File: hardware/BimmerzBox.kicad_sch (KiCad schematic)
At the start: 1 part, among them U2 ESP32-P4_MODULE

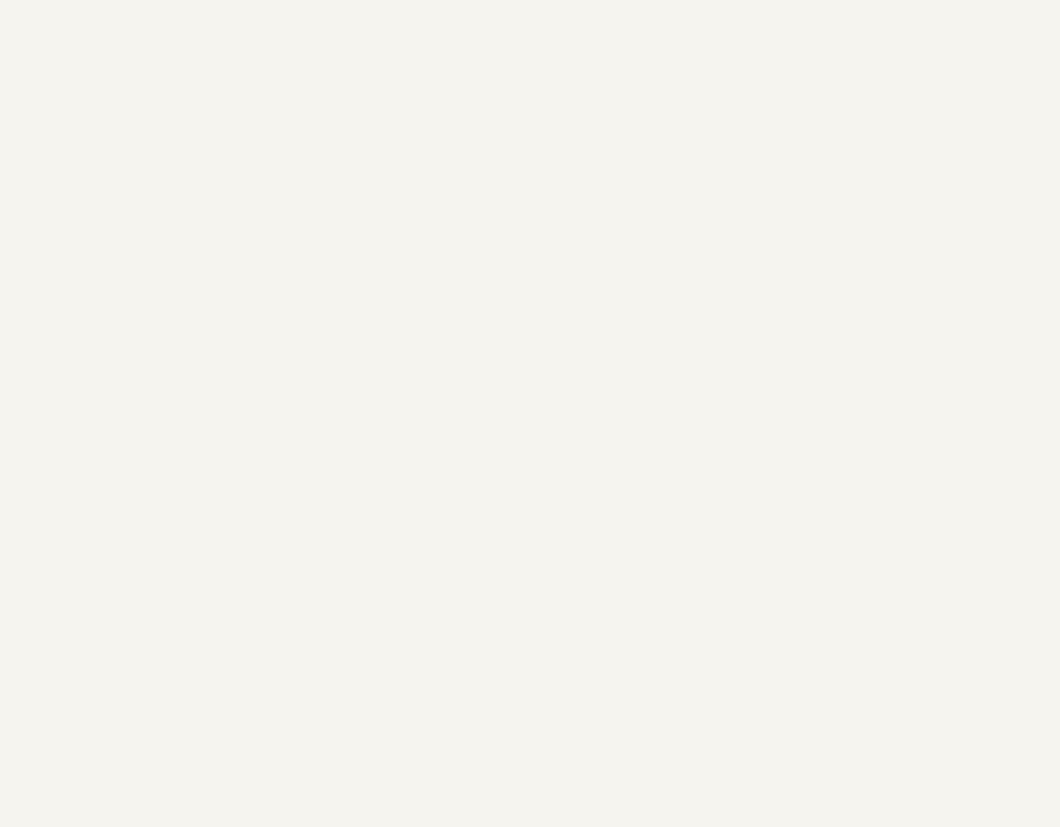
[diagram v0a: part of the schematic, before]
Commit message: hardware: schematic capture + custom footprint library
Bulks out the BimmerzBox.kicad_sch with the actual schematic capture
work — power tree (12 V → 3.3 V), Waveshare ESP32-P4 Module
connections, K-line front-end (L9637D + TMUX1208), dual CAN
(TJA1051T ×2), USB-C, SD socket, status LEDs.

Adds a project-local KiCad footprint library (hardware/Various.pretty)
with:
  - L9637D — BMW-grade K-line transceiver
  - COMTECH_C-OBD-II-16M — board-mount 16-pin OBD-II receptacle
  - Untitled.kicad_mod — WIP footprint, to be named

fp-lib-table wires the Various library into the project so
fab-output passes resolve cleanly.
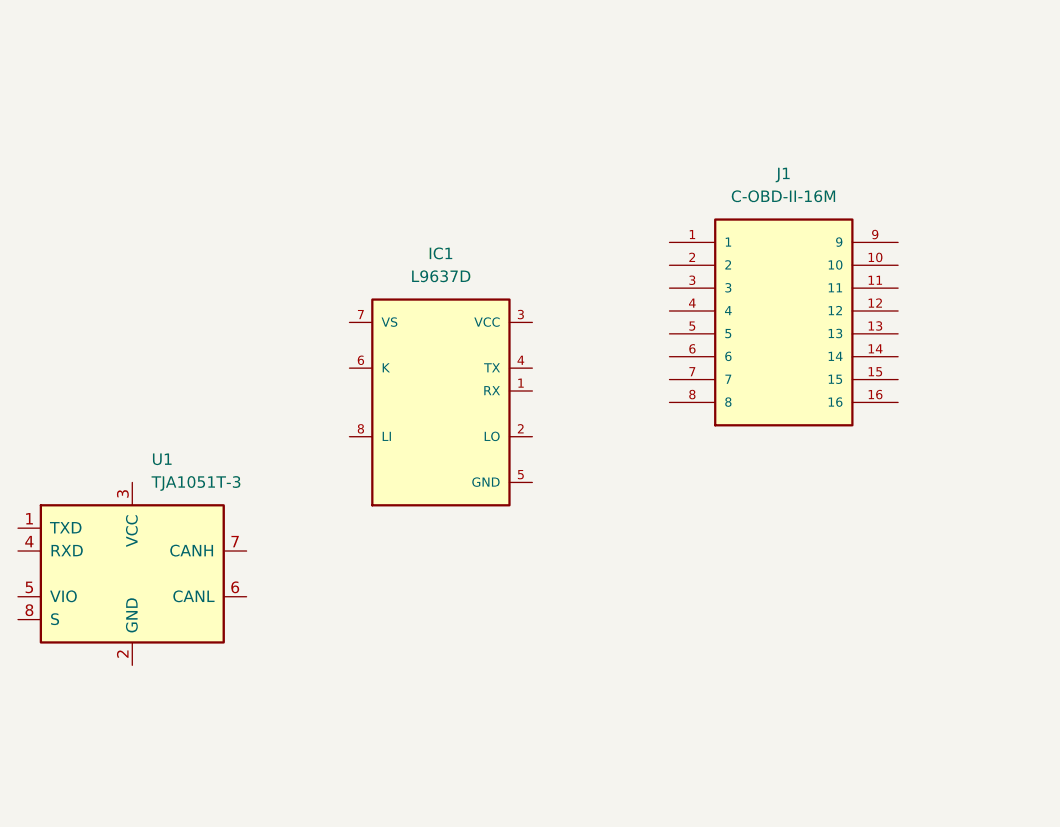
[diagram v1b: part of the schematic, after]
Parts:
- added IC1: L9637D, L9637D:SO08, symbol L9637D:L9637D
- added J1: C-OBD-II-16M, C-OBD-II-16M:COMTECH_C-OBD-II-16M, symbol C-OBD-II-16M:C-OBD-II-16M
- added U1: TJA1051T-3, Package_SO:SOIC-8_3.9x4.9mm_P1.27mm, symbol Interface_CAN_LIN:TJA1051T-3
